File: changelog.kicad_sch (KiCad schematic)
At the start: 0 parts

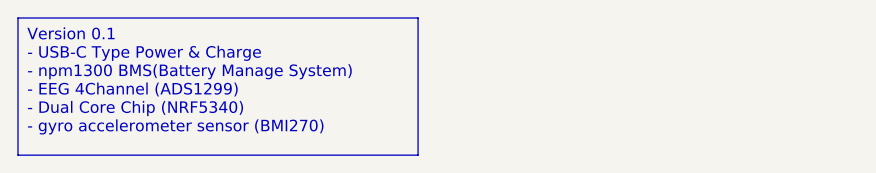
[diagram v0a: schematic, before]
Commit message: Feat: 개발보드 버전으로 PCB 변경
수정사항

단가 감소
- PCB Board size up (50x50)
- blind via 제거 (전체 레이아웃 수정)
- AVDD 전력평면 추가
- ADS1299 안쓰는핀 GND
- ADS1299 배치 변경 (Layout Reference 적용)

개발보드만 적용사항
- Pin Header size up 1.27 → 2.54mm
- PCB Size 50x50(mm)
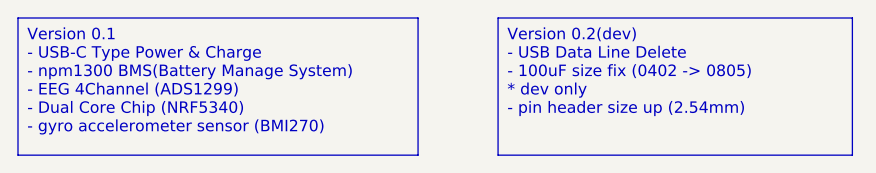
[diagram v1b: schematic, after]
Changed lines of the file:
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@@
 	(generator_version "8.0")
 	(paper "A4")
+	(text_box "Version 0.2(dev)\n- USB Data Line Delete\n- 100uF size fix (0402 -> 0805)\n* dev only\n- pin header size up (2.54mm)"
+		(exclude_from_sim no)
+		(at 67.31 13.97 0)
+		(size 39.37 15.24)
+		(stroke
+			(width 0)
+			(type default)
+		)
+		(fill
+			(type none)
+		)
+		(effects
+			(font
+				(size 1.27 1.27)
+			)
+			(justify left top)
+		)
+	)
 	(text_box "Version 0.1\n- USB-C Type Power & Charge\n- npm1300 BMS(Battery Manage System)\n- EEG 4Channel (ADS1299)\n- Dual Core Chip (NRF5340)\n- gyro accelerometer sensor (BMI270)"
 		(exclude_from_sim no)
